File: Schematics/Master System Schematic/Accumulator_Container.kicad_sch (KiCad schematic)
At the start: 16 parts, among them J5 Main TS Connector, J7 Radiator Fan Connector, J8 GLV Connector, J9 TSMP Connector, M10 Fan_4pin, M11 Fan_4pin, M4 Fan_4pin, M5 Fan_4pin, M6 Fan_4pin, M7 Fan_4pin, M8 Fan_4pin, M9 Fan_4pin, SW11 SMD_1, SW12 HVD, SW13 SMD_2

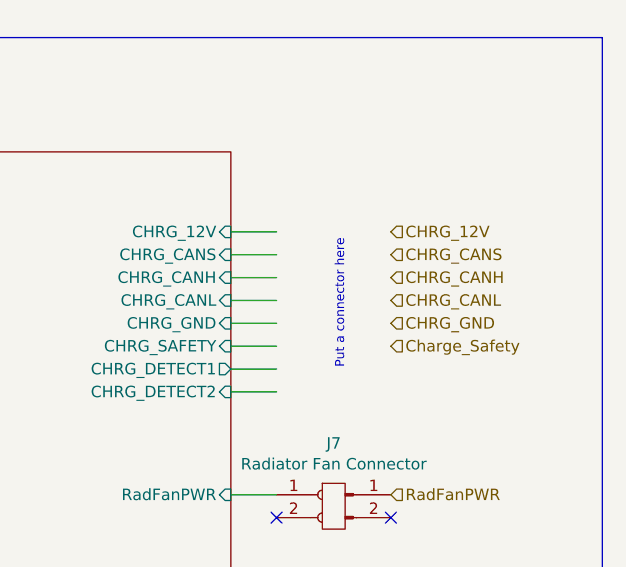
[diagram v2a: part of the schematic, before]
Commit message: Added charge connector and charge detection
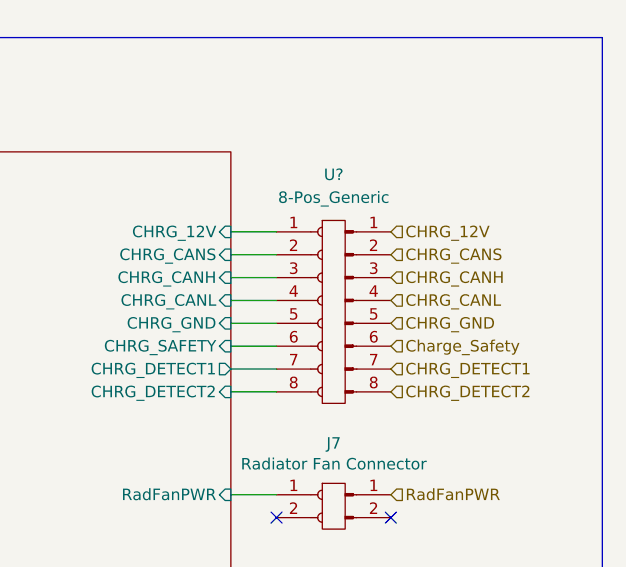
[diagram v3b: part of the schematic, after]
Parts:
- added U?: 8-Pos_Generic, symbol NER:8-Pos_Generic
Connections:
- net CHRG_12V: now also U?.1
- net CHRG_CANH: now also U?.3
- net CHRG_CANL: now also U?.4
- net CHRG_CANS: now also U?.2
- net CHRG_GND: now also U?.5
- net Charge_Safety: now also U?.6
- net LV_Plate/CHRG_12V: now also U?.1
- net LV_Plate/CHRG_CANH: now also U?.3
- net LV_Plate/CHRG_CANL: now also U?.4
- net LV_Plate/CHRG_CANS: now also U?.2
- net LV_Plate/CHRG_DETECT1: now also U?.7
- net LV_Plate/CHRG_DETECT2: now also U?.8
- net LV_Plate/CHRG_GND: now also U?.5
- net LV_Plate/CHRG_SAFETY: now also U?.6
- new net CHRG_DETECT1: U?.7
- new net CHRG_DETECT2: U?.8
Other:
- note removed: "Put a connector here"
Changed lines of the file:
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@@
     (effects (font (size 1.27 1.27)) (justify right bottom))
-  )
-  (text "Put a connector here" (at 369.57 62.23 90)
-    (effects (font (size 1 1)) (justify left bottom))
   )
   (hierarchical_label "CHRG_CANH" (shape input) (at 374.65 52.07 0)
@@
     (effects (font (size 1.27 1.27)) (justify right))
   )
+  (hierarchical_label "CHRG_DETECT1" (shape input) (at 374.65 62.23 0)
+    (effects (font (size 1.27 1.27)) (justify left))
+  )
   (hierarchical_label "CHRG_CANS" (shape input) (at 374.65 49.53 0)
     (effects (font (size 1.27 1.27)) (justify left))
@@
   )
   (hierarchical_label "GLV_CANH" (shape input) (at 374.65 99.06 0)
+    (effects (font (size 1.27 1.27)) (justify left))
+  )
+  (hierarchical_label "CHRG_DETECT2" (shape input) (at 374.65 64.77 0)
     (effects (font (size 1.27 1.27)) (justify left))
   )
@@
     (pin "2")
   )
+  (symbol (lib_id "NER:8-Pos_Generic") (at 368.3 43.18 0) (unit 1)
+    (in_bom yes) (on_board yes) (fields_autoplaced)
+    (property "Reference" "U?" (id 0) (at 368.3 40.64 0))
+    (property "Value" "8-Pos_Generic" (id 1) (at 368.3 43.18 0))
+    (property "Footprint" "" (id 2) (at 368.3 43.18 0)
+      (effects (font (size 1.27 1.27)) hide)
+    )
+    (property "Datasheet" "" (id 3) (at 368.3 43.18 0)
+      (effects (font (size 1.27 1.27)) hide)
+    )
+    (pin "1")
+    (pin "1")
+    (pin "2")
+    (pin "2")
+    (pin "3")
+    (pin "3")
+    (pin "4")
+    (pin "4")
+    (pin "5")
+    (pin "5")
+    (pin "6")
+    (pin "6")
+    (pin "7")
+    (pin "7")
+    (pin "8")
+    (pin "8")
+  )
   (sheet (at 306.07 38.1) (size 50.8 144.78) (fields_autoplaced)

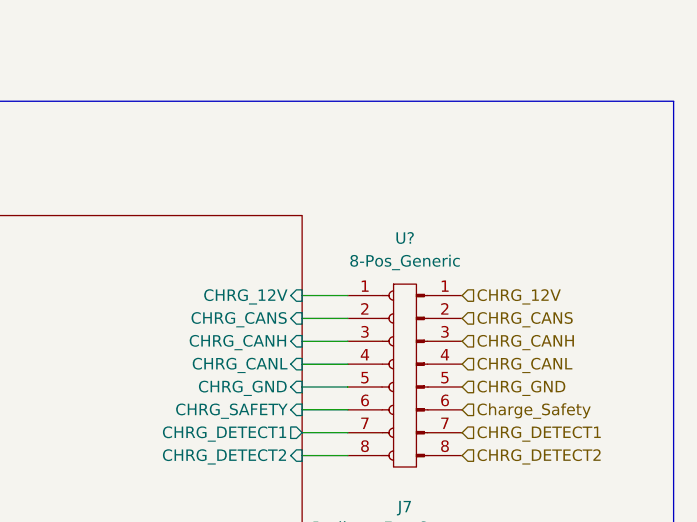
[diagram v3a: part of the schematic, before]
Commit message: Moved Side BRB
Returned to pre fuse box location
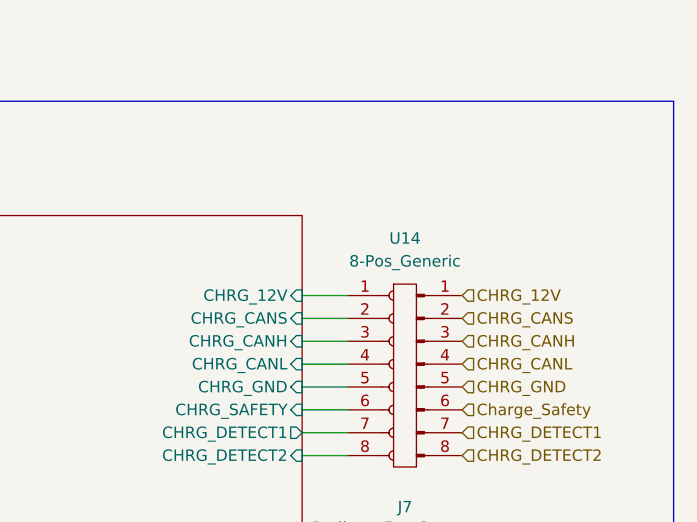
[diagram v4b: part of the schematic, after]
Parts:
- gave numbers to parts that had none: 1
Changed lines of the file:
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@@
   (symbol (lib_id "NER:8-Pos_Generic") (at 368.3 43.18 0) (unit 1)
     (in_bom yes) (on_board yes) (fields_autoplaced)
-    (property "Reference" "U?" (id 0) (at 368.3 40.64 0))
+    (property "Reference" "U14" (id 0) (at 368.3 40.64 0))
     (property "Value" "8-Pos_Generic" (id 1) (at 368.3 43.18 0))
     (property "Footprint" "" (id 2) (at 368.3 43.18 0)

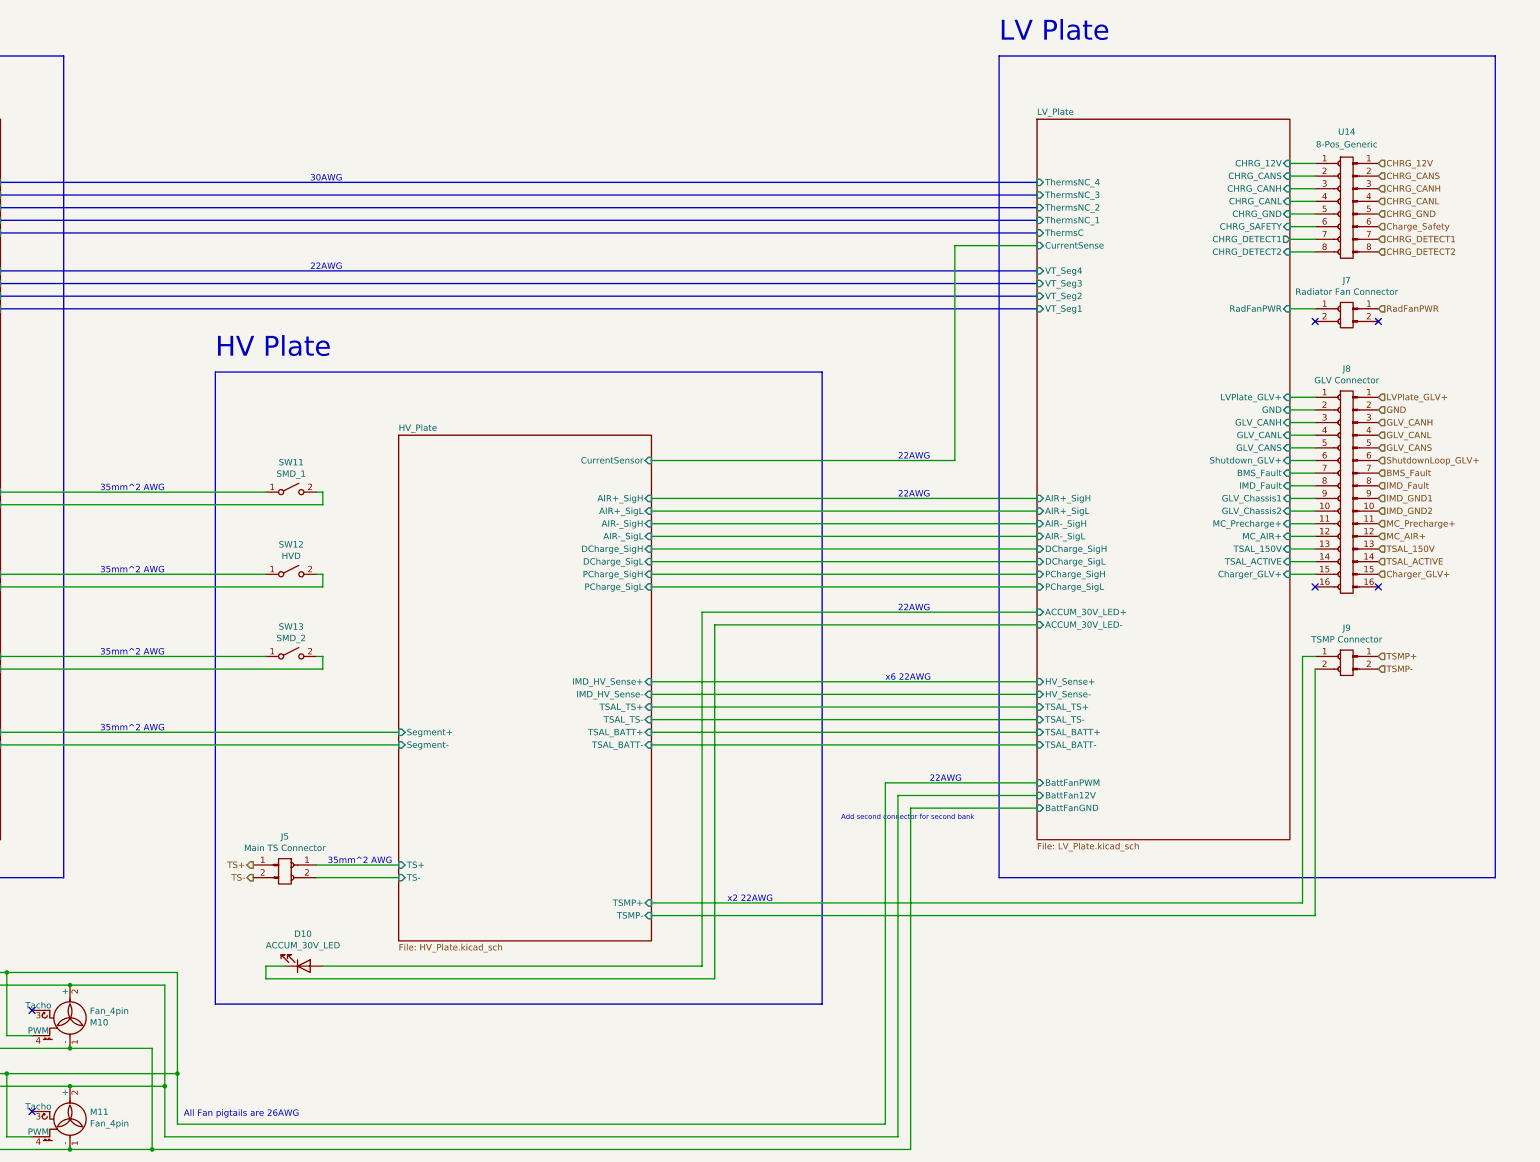
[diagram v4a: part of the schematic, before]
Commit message: Hubert and raajas color coding (#129)
* Charger Wiring Color Code and Wiring Update

Color Coded Wires. Updated wire gauges, added fans and CAN resistor

* Update to accumulator and charger

Update to accumulator and charger color coding

* Master schematic colour coded

* Added 2AWG to colour coding legend

* Update color coding

Update color coding accumulator stuff

* Added wire colours next to legend

* Update for color coding

Update for color coding

* update color and add fan

update color and add fan

* further update

further update

* more update

* more update

more update

* change again

change again

Co-authored-by: Raajas <52158581+Litmusblox@users.noreply.github.com>
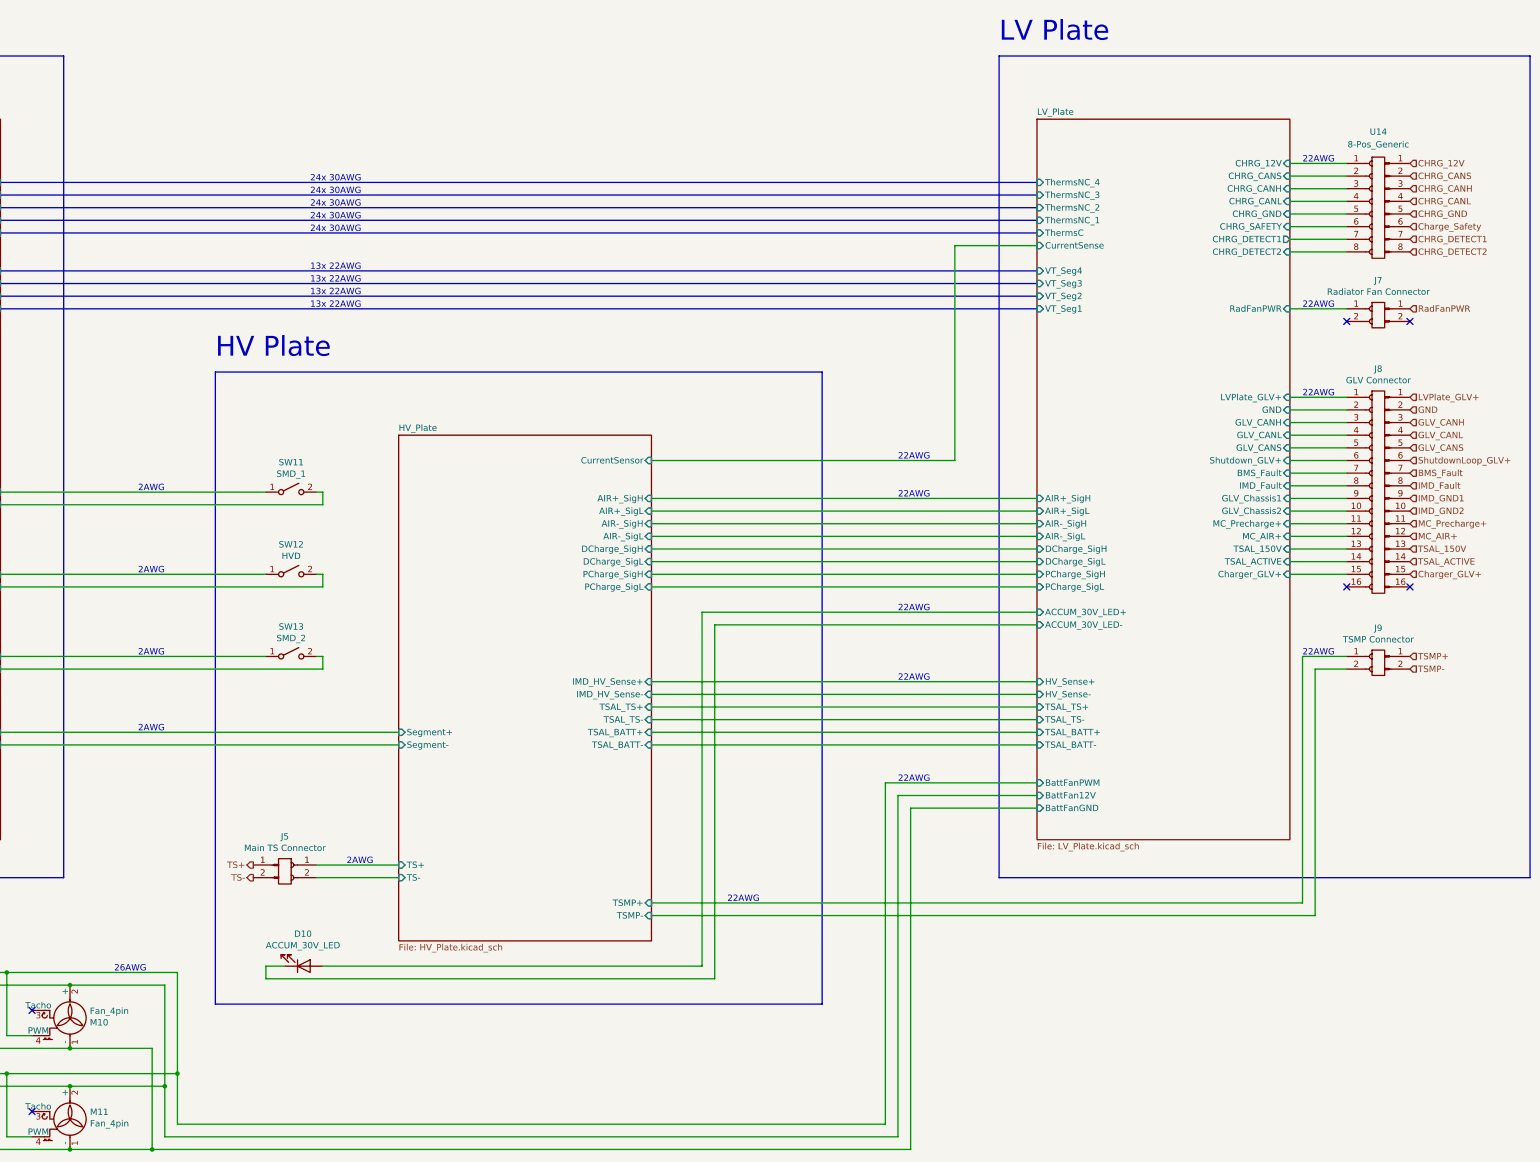
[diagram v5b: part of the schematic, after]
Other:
- note added: "13x 22AWG"
- note added: "24x 30AWG"
- note added: "26AWG"
- note added: "2AWG"
- note removed: "30AWG"
- note removed: "35mm^2 AWG"
- note removed: "Add second connector for second bank"
- note removed: "All Fan pigtails are 26AWG"
- note removed: "x2 22AWG"
- note removed: "x6 22AWG"
- moved on the sheet: J7, J8, J9, U14

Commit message: Matt final comp updates (#130)
* Master schematic fixes

- readded charge backpower
- Added Driver io LV batt guage
- Thickened wires
- swapped 2awg to 35mm2

* Exporting

* TS main fuse

Changed from 200 to 175

* Fixed sheet size

* Updated charger wire guage

thicc

* Fixed footwell sheet
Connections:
- net RadFanPWR is gone; now on net LV_Plate/RadFanPWR: J7.1
- no-connect marks 11 -> 12
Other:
- note added: "35mm^2"
- note removed: "2AWG"
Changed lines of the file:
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@@
   )
   (no_connect (at 104.14 217.17))
+  (no_connect (at 381 76.2))
   (no_connect (at 77.47 237.49))
   (no_connect (at 77.47 217.17))
@@
   (no_connect (at 50.8 237.49))
   (wire (pts (xy 161.29 113.03) (xy 162.56 113.03))
-    (stroke (width 0) (type default) (color 221 133 0 1))
+    (stroke (width 1) (type default) (color 221 133 0 1))
   )
   (wire (pts (xy 45.72 209.55) (xy 72.39 209.55))
@@
   )
   (wire (pts (xy 97.79 148.59) (xy 162.56 148.59))
-    (stroke (width 0) (type default) (color 221 133 0 1))
+    (stroke (width 1) (type default) (color 221 133 0 1))
   )
   (wire (pts (xy 368.3 146.05) (xy 359.41 146.05))
@@
   )
   (wire (pts (xy 161.29 190.5) (xy 177.8 190.5))
-    (stroke (width 0) (type default) (color 221 133 0 1))
+    (stroke (width 1) (type default) (color 221 133 0 1))
   )
   (polyline (pts (xy 21.59 190.5) (xy 21.59 25.4))
@@
   )
   (wire (pts (xy 97.79 132.08) (xy 162.56 132.08))
-    (stroke (width 0) (type default) (color 221 133 0 1))
+    (stroke (width 1) (type default) (color 221 133 0 1))
   )
   (wire (pts (xy 289.56 63.5) (xy 306.07 63.5))
@@
   )
   (wire (pts (xy 97.79 113.03) (xy 151.13 113.03))
-    (stroke (width 0) (type default) (color 221 133 0 1))
+    (stroke (width 1) (type default) (color 221 133 0 1))
   )
   (wire (pts (xy 228.6 156.21) (xy 306.07 156.21))
@@
   )
   (wire (pts (xy 177.8 187.96) (xy 161.29 187.96))
-    (stroke (width 0) (type default) (color 221 133 0 1))
+    (stroke (width 1) (type default) (color 221 133 0 1))
   )
   (wire (pts (xy 361.95 198.12) (xy 361.95 148.59))
@@
   )
   (wire (pts (xy 97.79 129.54) (xy 151.13 129.54))
-    (stroke (width 0) (type default) (color 221 133 0 1))
+    (stroke (width 1) (type default) (color 221 133 0 1))
   )
   (polyline (pts (xy 110.49 190.5) (xy 21.59 190.5))
@@
   )
   (wire (pts (xy 97.79 146.05) (xy 151.13 146.05))
-    (stroke (width 0) (type default) (color 221 133 0 1))
+    (stroke (width 1) (type default) (color 221 133 0 1))
   )
   (wire (pts (xy 130.81 232.41) (xy 130.81 212.09))
@@
   )
   (wire (pts (xy 97.79 163.83) (xy 177.8 163.83))
-    (stroke (width 0) (type default) (color 221 133 0 1))
+    (stroke (width 1) (type default) (color 221 133 0 1))
   )
   (wire (pts (xy 368.3 52.07) (xy 356.87 52.07))
@@
   )
   (wire (pts (xy 97.79 115.57) (xy 162.56 115.57))
-    (stroke (width 0) (type default) (color 221 133 0 1))
+    (stroke (width 1) (type default) (color 221 133 0 1))
   )
   (wire (pts (xy 306.07 124.46) (xy 228.6 124.46))
@@
   )
   (wire (pts (xy 162.56 148.59) (xy 162.56 146.05))
-    (stroke (width 0) (type default) (color 221 133 0 1))
+    (stroke (width 1) (type default) (color 221 133 0 1))
   )
   (wire (pts (xy 151.13 208.28) (xy 151.13 210.82))
@@
   )
   (wire (pts (xy 162.56 129.54) (xy 162.56 132.08))
-    (stroke (width 0) (type default) (color 221 133 0 1))
+    (stroke (width 1) (type default) (color 221 133 0 1))
   )
   (wire (pts (xy 133.35 229.87) (xy 133.35 209.55))
@@
   )
   (wire (pts (xy 162.56 113.03) (xy 162.56 115.57))
-    (stroke (width 0) (type default) (color 221 133 0 1))
+    (stroke (width 1) (type default) (color 221 133 0 1))
   )
   (wire (pts (xy 99.06 229.87) (xy 133.35 229.87))
@@
   )
   (wire (pts (xy 177.8 161.29) (xy 97.79 161.29))
-    (stroke (width 0) (type default) (color 221 133 0 1))
+    (stroke (width 1) (type default) (color 221 133 0 1))
   )
   (wire (pts (xy 72.39 222.25) (xy 72.39 209.55))
@@
   )
   (wire (pts (xy 162.56 146.05) (xy 161.29 146.05))
-    (stroke (width 0) (type default) (color 221 133 0 1))
+    (stroke (width 1) (type default) (color 221 133 0 1))
   )
   (wire (pts (xy 228.6 116.84) (xy 306.07 116.84))
@@
   )
   (wire (pts (xy 161.29 129.54) (xy 162.56 129.54))
-    (stroke (width 0) (type default) (color 221 133 0 1))
+    (stroke (width 1) (type default) (color 221 133 0 1))
   )
   (text "22AWG" (at 278.13 171.45 0)
@@
     (effects (font (size 3.9878 3.9878)) (justify left bottom))
   )
-  (text "2AWG" (at 130.81 146.05 180)
-    (effects (font (size 1.27 1.27)) (justify right bottom))
+  (text "35mm^2" (at 166.37 186.69 0)
+    (effects (font (size 1.27 1.27)) (justify left bottom))
   )
   (text "24x 30AWG" (at 160.02 55.88 0)
@@
     (effects (font (size 1.27 1.27)) (justify left bottom))
   )
+  (text "35mm^2" (at 125.095 145.415 0)
+    (effects (font (size 1.27 1.27)) (justify left bottom))
+  )
   (text "22AWG\n" (at 359.41 93.98 0)
     (effects (font (size 1.27 1.27)) (justify left bottom))
   )
   (text "22AWG" (at 278.13 151.13 0)
+    (effects (font (size 1.27 1.27)) (justify left bottom))
+  )
+  (text "35mm^2" (at 124.46 160.655 0)
     (effects (font (size 1.27 1.27)) (justify left bottom))
   )
@@
     (effects (font (size 1.27 1.27)) (justify left bottom))
   )
-  (text "2AWG" (at 172.72 187.96 180)
-    (effects (font (size 1.27 1.27)) (justify right bottom))
-  )
   (text "22AWG" (at 278.13 137.16 0)
     (effects (font (size 1.27 1.27)) (justify left bottom))
   )
-  (text "2AWG" (at 130.81 129.54 180)
-    (effects (font (size 1.27 1.27)) (justify right bottom))
-  )
   (text "13x 22AWG" (at 160.02 71.12 0)
     (effects (font (size 1.27 1.27)) (justify left bottom))
@@
     (effects (font (size 1.27 1.27)) (justify left bottom))
   )
-  (text "2AWG" (at 130.81 161.29 180)
-    (effects (font (size 1.27 1.27)) (justify right bottom))
-  )
   (text "22AWG" (at 278.13 106.68 0)
     (effects (font (size 1.27 1.27)) (justify left bottom))
   )
-  (text "2AWG" (at 130.81 113.03 180)
-    (effects (font (size 1.27 1.27)) (justify right bottom))
-  )
   (text "24x 30AWG" (at 160.02 53.34 0)
     (effects (font (size 1.27 1.27)) (justify left bottom))
   )
+  (text "35mm^2" (at 126.365 128.905 0)
+    (effects (font (size 1.27 1.27)) (justify left bottom))
+  )
   (text "22AWG\n" (at 359.41 76.2 0)
+    (effects (font (size 1.27 1.27)) (justify left bottom))
+  )
+  (text "35mm^2" (at 126.365 112.395 0)
     (effects (font (size 1.27 1.27)) (justify left bottom))
   )
@@
     (effects (font (size 1.27 1.27)) (justify left))
   )
-  (hierarchical_label "RadFanPWR" (shape input) (at 381 76.2 0)
-    (effects (font (size 1.27 1.27)) (justify left))
-  )
